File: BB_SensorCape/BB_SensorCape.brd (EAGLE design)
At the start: 54.6 x 71.8 mm, 40 parts, among them U1 FGPMMOPA6H, U2 MAX232SOIC16

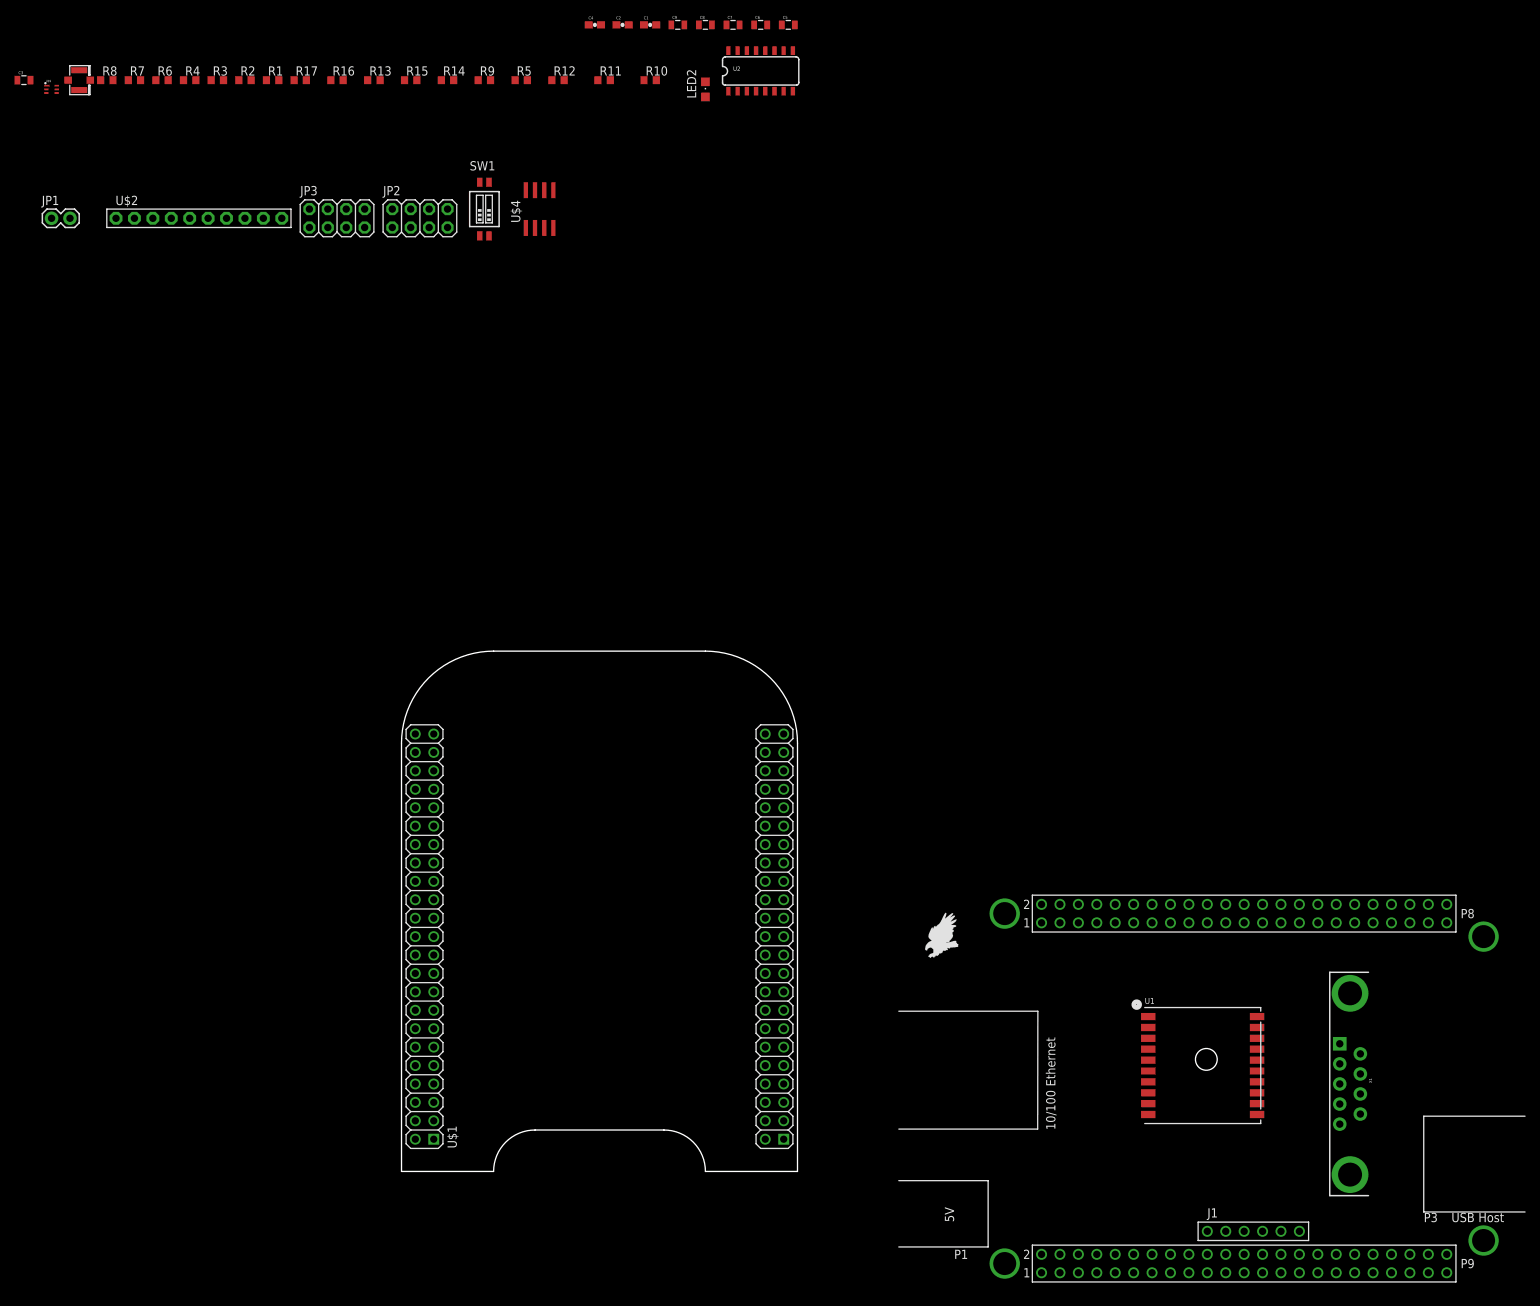
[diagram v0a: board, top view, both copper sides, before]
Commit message: Schematic/Board updates 01/03
Minor updates over holiday break
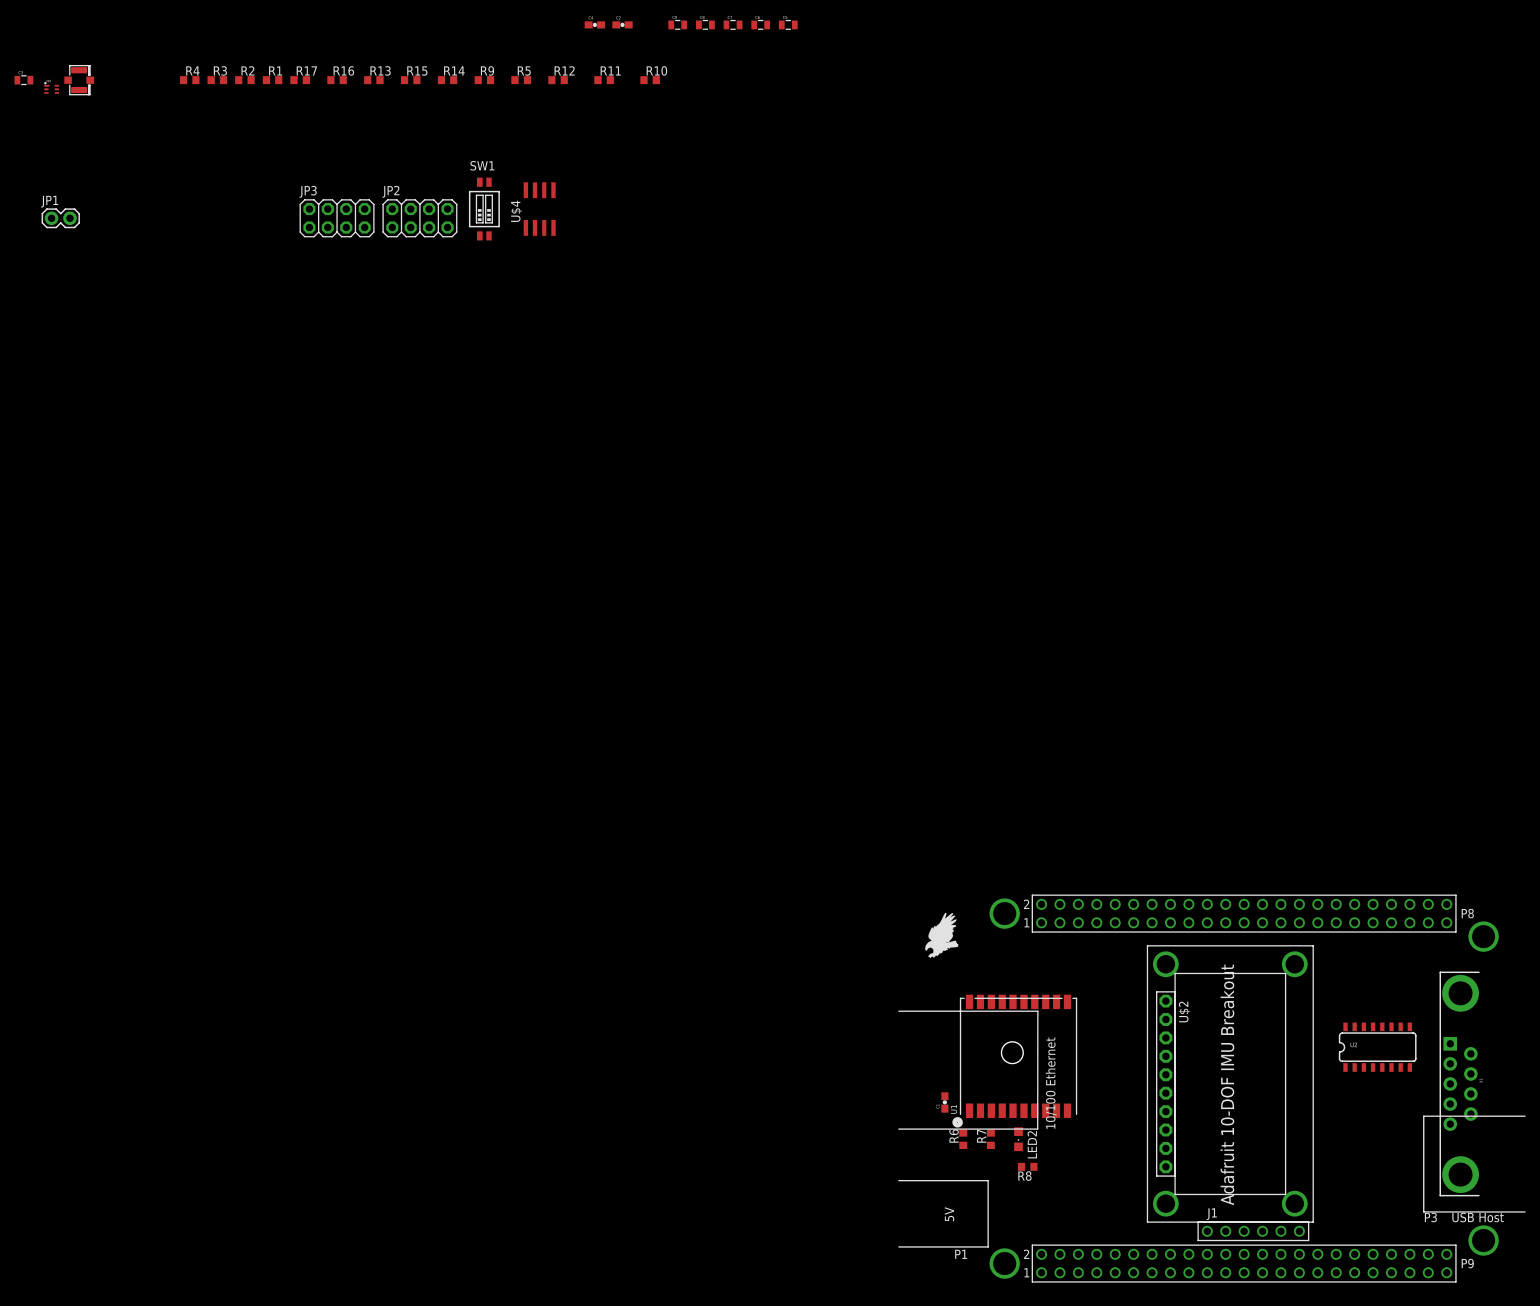
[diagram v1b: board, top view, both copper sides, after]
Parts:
- removed U$1: BEAGLEBONE_OUTLINE, adafruit:BEAGLEBONE_SHIELD
- moved R8 196.4 mm to (17.8, 16.5), turned to 180 degrees
- moved R7 187.8 mm to (12.7, 20.3), turned to 90 degrees
- moved R6 183.1 mm to (8.89, 20.3), turned to 90 degrees
- moved U$2 179.0 mm to (36.8, 27.9), turned to 270 degrees
- moved U2 159.3 mm to (66.0, 33.0)
- moved C1 154.0 mm to (6.35, 25.4), turned to 90 degrees
- moved LED2 151.1 mm to (16.5, 20.3), turned to 180 degrees
- moved U1 25.4 mm to (16.5, 31.8), turned to 90 degrees
- moved X1 15.2 mm to (77.5, 27.9)
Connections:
- removed net AIN0: U$1.85
- removed net SYS_5V: U$1.53
- net 1PPS: now also PCB1.P9.15; no longer U$1.61
- net 3.3V: no longer U$1.49, U$1.50
- net 5V: no longer U$1.51, U$1.52
- net BB_GPS_RX: now also PCB1.P9.26; no longer U$1.72
- net BB_GPS_TX: now also PCB1.P9.24; no longer U$1.70
- net DBG_RX: now also PCB1.P9.22; no longer U$1.68
- net DBG_TX: now also PCB1.P9.21; no longer U$1.67
- net GND: no longer U$1.1, U$1.2, U$1.47, U$1.48, U$1.89, U$1.90, U$1.91, U$1.92
- net GPS_FIX: now also PCB1.P8.45; no longer U$1.45
- net GPS_NRESET: now also PCB1.P9.12; no longer U$1.58
- net GYR_INT: now also PCB1.P8.39; no longer U$1.39
- net GYR_RDY: now also PCB1.P8.41; no longer U$1.41
- net I2C2_SCL: now also PCB1.P9.19; no longer U$1.65
- net I2C2_SDA: now also PCB1.P9.20; no longer U$1.66
- net ISL29125_INT: now also PCB1.P8.44; no longer U$1.44
- net LSM_DRDY: now also PCB1.P8.42; no longer U$1.42
- net LSM_INT1: now also PCB1.P8.43; no longer U$1.43
- net LSM_INT2: now also PCB1.P8.40; no longer U$1.40
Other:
- board outline removed
- board text added: "Adafruit 10-DOF IMU Breakout"

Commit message: Board updates 01/04
routing at ~98%
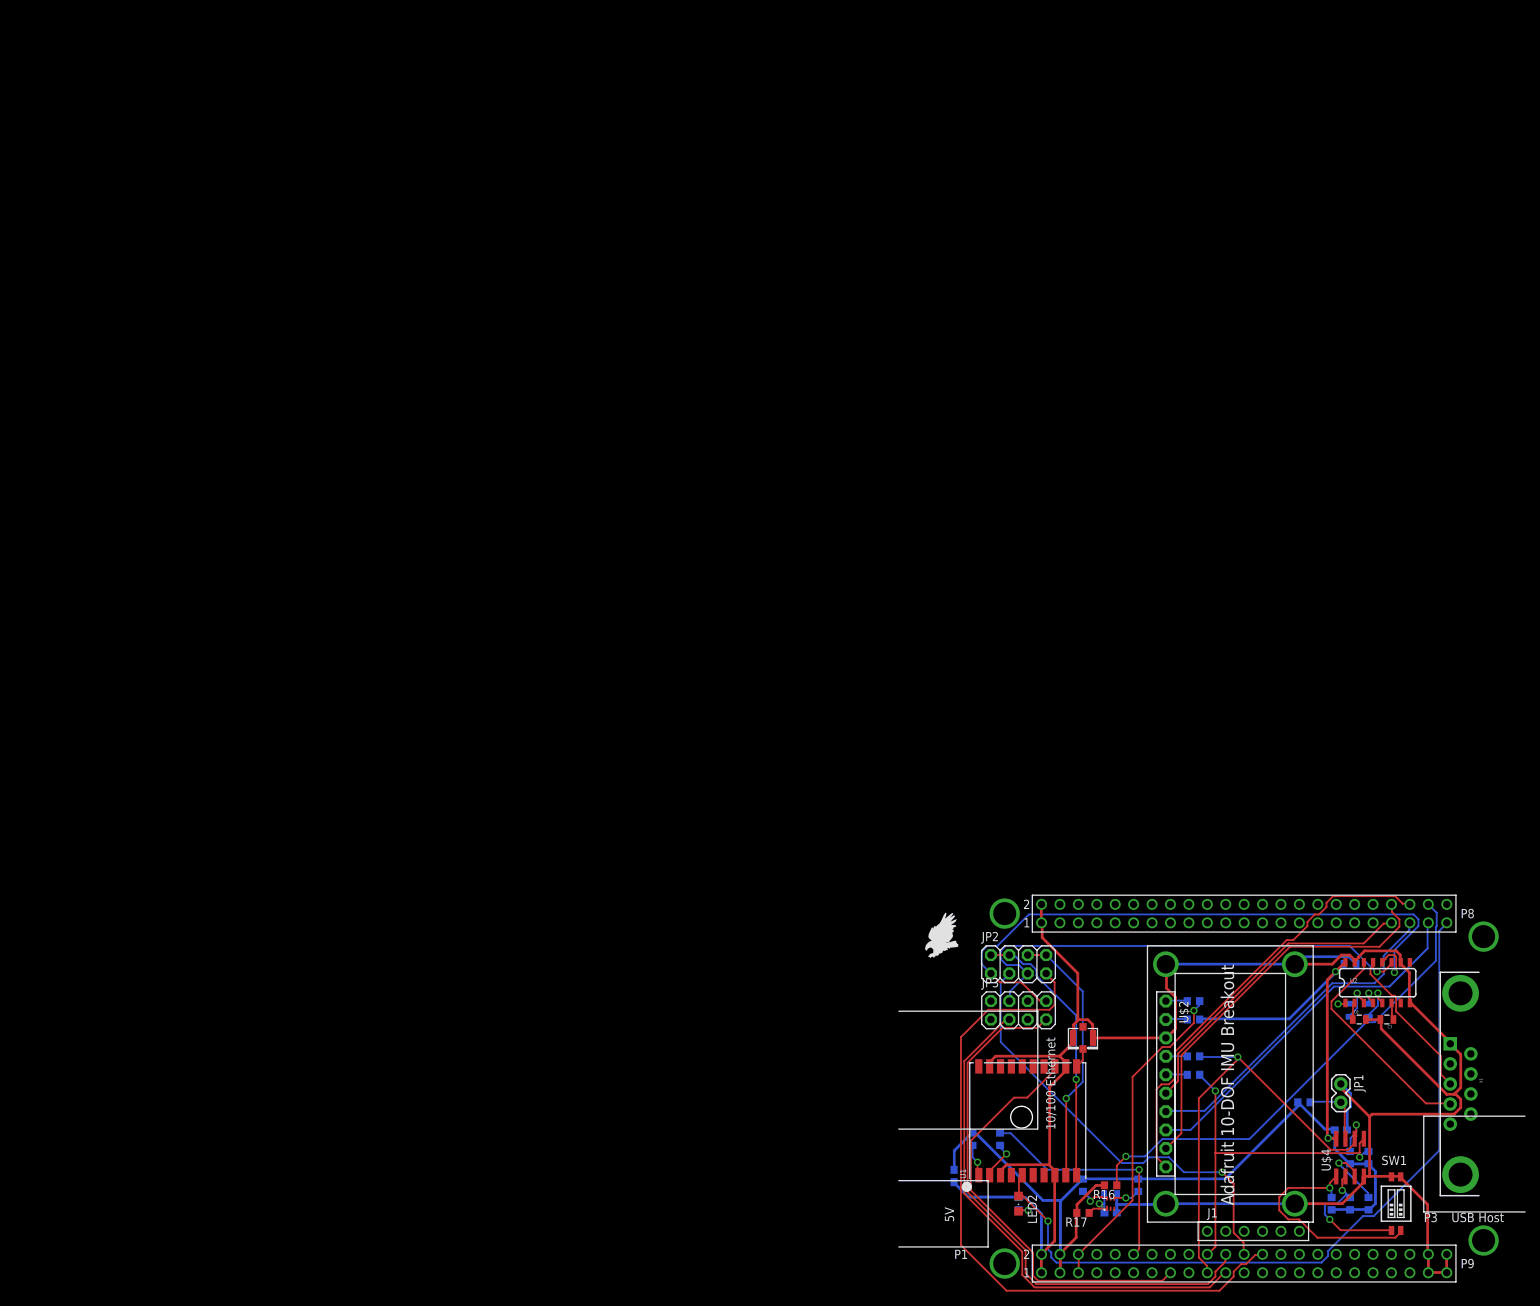
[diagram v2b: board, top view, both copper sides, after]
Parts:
- moved C3 214.6 mm to (29.2, 12.7), flipped to the bottom, turned to 180 degrees
- moved JP1 214.2 mm to (61.0, 27.9), turned to 270 degrees
- moved U$9 212.0 mm to (29.2, 11.4), turned to 90 degrees
- moved R4 194.9 mm to (40.6, 29.2), flipped to the bottom
- moved R9 192.2 mm to (64.8, 17.8), flipped to the bottom, turned to 270 degrees
- moved U$20 191.3 mm to (25.4, 34.3), turned to 270 degrees
- moved R13 190.6 mm to (55.9, 25.4), flipped to the bottom
- moved R3 190.4 mm to (40.6, 31.8), flipped to the bottom
- moved R17 189.9 mm to (25.4, 10.2), turned to 180 degrees
- moved R12 188.1 mm to (59.7, 11.4), flipped to the bottom, turned to 270 degrees
- moved R5 187.5 mm to (62.2, 17.8), flipped to the bottom, turned to 270 degrees
- moved SW1 186.1 mm to (68.6, 11.4)
- moved R16 186.0 mm to (29.2, 14.0), turned to 180 degrees
- moved R11 186.0 mm to (62.2, 11.4), flipped to the bottom, turned to 270 degrees
- moved R2 184.1 mm to (40.6, 36.8), flipped to the bottom
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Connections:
- net 3.3V: now also R13.2
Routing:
- net GND: track 0.00 -> 304.4 mm
- net 3.3V: track 0.00 -> 161.4 mm, vias 0 -> 2
- net GPS_FIX: track 0.00 -> 106.3 mm, vias 0 -> 1
- net BB_GPS_RX: track 0.00 -> 94.9 mm
- net RXD: track 0.00 -> 88.8 mm, vias 0 -> 1
- net DBG_RX: track 0.00 -> 76.5 mm
- net DBG_TX: track 0.00 -> 71.0 mm
- net TXD: track 0.00 -> 66.8 mm, vias 0 -> 1
- net ISL29125_INT: track 0.00 -> 66.7 mm, vias 0 -> 1
- net I2C2_SCL: track 0.00 -> 66.3 mm, vias 0 -> 2
- net BB_GPS_TX: track 0.00 -> 61.2 mm, vias 0 -> 1
- net LSM_DRDY: track 0.00 -> 60.5 mm
- net 1PPS: track 0.00 -> 58.0 mm
- net LSM_INT2: track 0.00 -> 54.7 mm
- net I2C2_SDA: track 0.00 -> 50.4 mm, vias 0 -> 2
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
